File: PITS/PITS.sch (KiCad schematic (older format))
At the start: 48 parts, among them P1 CONN_02X20, P10 I2C, P11 I2C, P12 I2C, P13 I2C, P14 BATT, P2 BNC, P3 BNC, P4 BNC, P5 BNC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

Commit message: board - not finished
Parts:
- P2, P3, P4, P5, P6: footprint Connectors:bnc-ci -> Connectors:SMA_Edge
- U4, U6: footprint RF_Modules:PFM9x -> RF_Modules:RFM9xW
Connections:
- net GPIO12: now also U4.7 (DIO5); no longer U6.7 (DIO5)
- net GPIO16(CE2): now also U4.14 (DIO0); no longer U6.14 (DIO0)
- net GPIO24: now also U6.7 (DIO5); no longer U4.7 (DIO5)
- net GPIO25: now also U6.14 (DIO0); no longer U4.14 (DIO0)
- net GPIO7(CE1): now also U4.5 (nSS); no longer U6.5 (nSS)
- net GPIO8(CE0): now also U6.5 (nSS); no longer U4.5 (nSS)
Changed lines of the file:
@@
 F 0 "U4" H 5700 2350 60  0000 C CNN
 F 1 "RFM9*" H 5700 850 60  0000 C CNN
-F 2 "RF_Modules:PFM9x" H 5800 2800 60  0001 C CNN
+F 2 "RF_Modules:RFM9xW" H 5800 2800 60  0001 C CNN
 F 3 "" H 5800 2800 60  0001 C CNN
 	1    5700 1600
@@
 F 0 "P5" H 4910 1620 50  0000 C CNN
 F 1 "BNC" V 5010 1440 50  0000 C CNN
-F 2 "Connectors:bnc-ci" H 4900 1500 50  0001 C CNN
+F 2 "Connectors:SMA_Edge" H 4900 1500 50  0001 C CNN
 F 3 "" H 4900 1500 50  0000 C CNN
 	1    4900 1500
@@
 F 0 "U6" H 8200 2350 60  0000 C CNN
 F 1 "RFM9*" H 8200 850 60  0000 C CNN
-F 2 "RF_Modules:PFM9x" H 8300 2800 60  0001 C CNN
+F 2 "RF_Modules:RFM9xW" H 8300 2800 60  0001 C CNN
 F 3 "" H 8300 2800 60  0001 C CNN
 	1    8200 1600
@@
 F 0 "P6" H 7410 1620 50  0000 C CNN
 F 1 "BNC" V 7510 1440 50  0000 C CNN
-F 2 "Connectors:bnc-ci" H 7400 1500 50  0001 C CNN
+F 2 "Connectors:SMA_Edge" H 7400 1500 50  0001 C CNN
 F 3 "" H 7400 1500 50  0000 C CNN
 	1    7400 1500
@@
 Text Label 9600 1100 2    60   ~ 0
 GPIO10(MOSI0)
+Text Label 9500 1300 2    60   ~ 0
+GPIO8(CE0)
 Text Label 7000 1300 2    60   ~ 0
-GPIO8(CE0)
-Text Label 9500 1300 2    60   ~ 0
 GPIO7(CE1)
+Text Label 9400 1500 2    60   ~ 0
+GPIO25
+Text Label 9400 2000 2    60   ~ 0
+GPIO24
+Text Label 6900 2000 2    60   ~ 0
+GPIO12
 Text Label 6900 1500 2    60   ~ 0
-GPIO25
-Text Label 6900 2000 2    60   ~ 0
-GPIO24
-Text Label 9400 2000 2    60   ~ 0
-GPIO12
-Text Label 9400 1500 2    60   ~ 0
 GPIO16(CE2)
 Text Notes 9650 2550 2    100  ~ 20
@@
 F 0 "P4" H 3710 6220 50  0000 C CNN
 F 1 "BNC" V 3810 6040 50  0000 C CNN
-F 2 "Connectors:bnc-ci" H 3700 6100 50  0001 C CNN
+F 2 "Connectors:SMA_Edge" H 3700 6100 50  0001 C CNN
 F 3 "" H 3700 6100 50  0000 C CNN
 	1    3700 6100
@@
 F 0 "P3" H 810 6120 50  0000 C CNN
 F 1 "BNC" V 910 5940 50  0000 C CNN
-F 2 "Connectors:bnc-ci" H 800 6000 50  0001 C CNN
+F 2 "Connectors:SMA_Edge" H 800 6000 50  0001 C CNN
 F 3 "" H 800 6000 50  0000 C CNN
 	1    800  6000
@@
 F 0 "P2" H 810 1120 50  0000 C CNN
 F 1 "BNC" V 910 940 50  0000 C CNN
-F 2 "Connectors:bnc-ci" H 800 1000 50  0001 C CNN
+F 2 "Connectors:SMA_Edge" H 800 1000 50  0001 C CNN
 F 3 "" H 800 1000 50  0000 C CNN
 	1    800  1000

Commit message: first finished layout
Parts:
- added U8: BME280, RF_Modules:BME280, symbol BME280
- C1, C14, C2, C4: footprint Capacitors_SMD:C_0805_HandSoldering -> Capacitors_SMD:C_0603_HandSoldering
- D1, D2, D3, D4, D5, D6: footprint LEDs:LED_0805 -> LEDs:LED_0603
- P14: footprint Connectors_Terminal_Blocks:TerminalBlock_Pheonix_MKDS1.5-2pol -> Connectors:SMD_2
- R1, R12, R13, R14, R15, R2, R20, R21, R22, R23, R24, R25, R26, R3, R4, R5, R8: footprint Resistors_SMD:R_0805_HandSoldering -> Resistors_SMD:R_0603_HandSoldering
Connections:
- net +3V3: now also U8.1 (Vin)
- net GND: now also U8.2 (GND)
- net GPIO12: now also U2.4 (TimePulse); no longer U4.7 (DIO5)
- net GPIO16(CE2): now also U2.16 (SDA); no longer U4.14 (DIO0)
- net GPIO19(MISO1): now also U2.17 (SCL); no longer R15.1
- net GPIO2(SDA1): now also U8.4 (SDA)
- net GPIO20(MOSI1): now also R15.1; no longer U2.4 (TimePulse)
- net GPIO22: now also U4.14 (DIO0); no longer U2.17 (SCL)
- net GPIO23: now also U6.7 (DIO5); no longer U1.4 (EN)
- net GPIO24: now also U6.14 (DIO0); no longer U6.7 (DIO5)
- net GPIO25: now also U1.4 (EN); no longer U6.14 (DIO0)
- net GPIO27: now also U4.7 (DIO5); no longer U2.16 (SDA)
- net GPIO3(SCL1): now also U8.3 (SCL)

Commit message: old layout - commit for backup
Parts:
- D3: value INTERNET_Green -> Inet_Green
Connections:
- net GPIO13: now also R21.1; no longer R20.1
- net GPIO16(CE2): now also U2.17 (SCL); no longer U2.16 (SDA)
- net GPIO19(MISO1): now also U2.16 (SDA); no longer U2.17 (SCL)
- net GPIO20(MOSI1): now also R20.1; no longer R15.1
- net GPIO26: now also R22.1; no longer R14.1
- net GPIO5: now also R14.1; no longer R22.1
- net GPIO6: now also R15.1; no longer R21.1
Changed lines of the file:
@@
 P 1200 3700
 F 0 "D3" H 1200 3800 50  0000 C CNN
-F 1 "INTERNET_Green" H 1200 3600 50  0000 C CNN
+F 1 "Inet_Green" H 1200 3600 50  0000 C CNN
 F 2 "LEDs:LED_0603" H 1200 3700 50  0001 C CNN
 F 3 "" H 1200 3700 50  0000 C CNN
@@
 	0    1    1    0
 $EndComp
+Text Label 2800 4500 2    60   ~ 0
+GPIO26
+Text Label 4300 1300 2    60   ~ 0
+GPIO19(MISO1)
+Text Label 2800 4100 2    60   ~ 0
+GPIO13
+Text Label 2800 3300 2    60   ~ 0
+GPIO6
 Text Label 2800 2900 2    60   ~ 0
-GPIO26
-Text Label 4300 1400 2    60   ~ 0
-GPIO19(MISO1)
-Text Label 2800 3700 2    60   ~ 0
-GPIO13
-Text Label 2800 4100 2    60   ~ 0
-GPIO6
-Text Label 2800 4500 2    60   ~ 0
 GPIO5
 Text Label 2800 4900 2    60   ~ 0
@@
 Text Label 3300 6200 2    60   ~ 0
 GPIO25
-Text Label 4300 1300 2    60   ~ 0
+Text Label 4300 1400 2    60   ~ 0
 GPIO16(CE2)
-Text Label 2800 3300 2    60   ~ 0
+Text Label 2800 3700 2    60   ~ 0
 GPIO20(MOSI1)
 Text Label 4100 1600 2    60   ~ 0

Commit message: working on layout
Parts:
- P2, P3, P4, P5, P6: footprint Connectors:SMA_Edge -> Connectors:SMA_Edge_small
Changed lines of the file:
@@
 F 0 "P5" H 4910 1620 50  0000 C CNN
 F 1 "BNC" V 5010 1440 50  0000 C CNN
-F 2 "Connectors:SMA_Edge" H 4900 1500 50  0001 C CNN
+F 2 "Connectors:SMA_Edge_small" H 4900 1500 50  0001 C CNN
 F 3 "" H 4900 1500 50  0000 C CNN
 	1    4900 1500
@@
 F 0 "P6" H 7410 1620 50  0000 C CNN
 F 1 "BNC" V 7510 1440 50  0000 C CNN
-F 2 "Connectors:SMA_Edge" H 7400 1500 50  0001 C CNN
+F 2 "Connectors:SMA_Edge_small" H 7400 1500 50  0001 C CNN
 F 3 "" H 7400 1500 50  0000 C CNN
 	1    7400 1500
@@
 F 0 "P4" H 3710 6220 50  0000 C CNN
 F 1 "BNC" V 3810 6040 50  0000 C CNN
-F 2 "Connectors:SMA_Edge" H 3700 6100 50  0001 C CNN
+F 2 "Connectors:SMA_Edge_small" H 3700 6100 50  0001 C CNN
 F 3 "" H 3700 6100 50  0000 C CNN
 	1    3700 6100
@@
 F 0 "P3" H 810 6120 50  0000 C CNN
 F 1 "BNC" V 910 5940 50  0000 C CNN
-F 2 "Connectors:SMA_Edge" H 800 6000 50  0001 C CNN
+F 2 "Connectors:SMA_Edge_small" H 800 6000 50  0001 C CNN
 F 3 "" H 800 6000 50  0000 C CNN
 	1    800  6000
@@
 F 0 "P2" H 810 1120 50  0000 C CNN
 F 1 "BNC" V 910 940 50  0000 C CNN
-F 2 "Connectors:SMA_Edge" H 800 1000 50  0001 C CNN
+F 2 "Connectors:SMA_Edge_small" H 800 1000 50  0001 C CNN
 F 3 "" H 800 1000 50  0000 C CNN
 	1    800  1000

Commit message: layout - work in progress
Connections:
- net D1: now reaches D1.2 (A), R14.2
- net D2: now reaches D2.2 (A), R15.2
- net D3: now reaches D3.2 (A), R20.2
- net D4: now reaches D4.2 (A), R21.2
- net D5: now reaches D5.2 (A), R22.2
- net D6: now reaches D6.2 (A), R23.2
- net MTX2-TXD: now reaches R2.1, R3.2, R4.2, U3.5 (TXD)
- net HX1-TXD: now reaches R26.2, U1.7 (TXD)
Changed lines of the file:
@@
 Wire Wire Line
 	1800 7300 2500 7300
+Text Label 5400 6000 0    30   ~ 0
+MTX2-TXD
+Text Label 2500 6100 0    30   ~ 0
+HX1-TXD
+Text Label 1500 2900 0    30   ~ 0
+D1
+Text Label 1500 3300 0    30   ~ 0
+D2
+Text Label 1500 3700 0    30   ~ 0
+D3
+Text Label 1500 4100 0    30   ~ 0
+D4
+Text Label 1500 4500 0    30   ~ 0
+D5
+Text Label 1500 4900 0    30   ~ 0
+D6
 $EndSCHEMATC

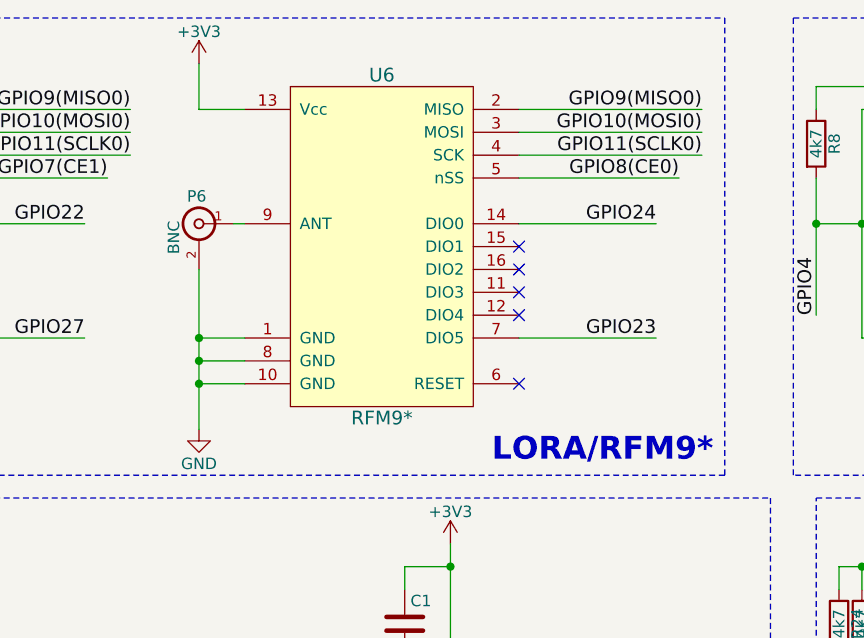
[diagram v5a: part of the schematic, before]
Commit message: layout for zero - work in progress - backup before pin header change
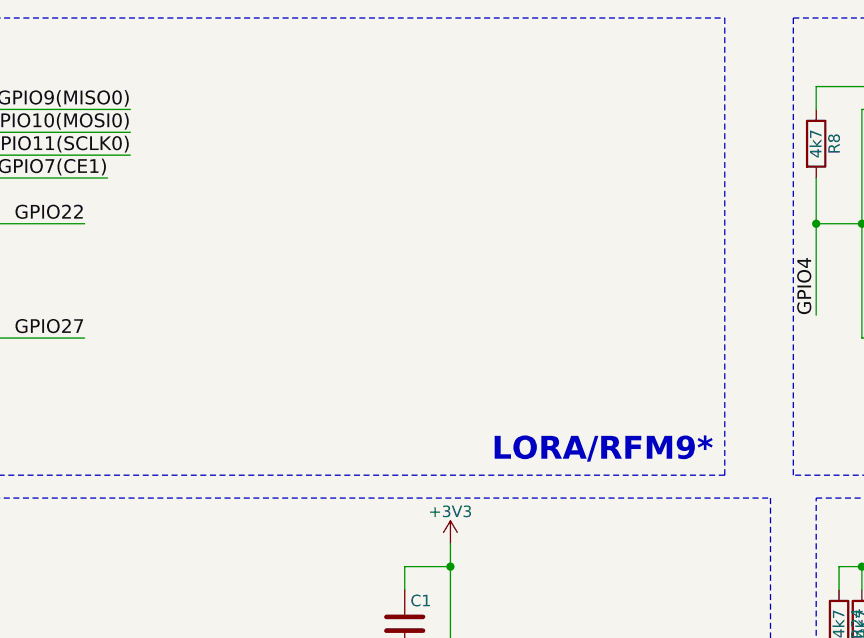
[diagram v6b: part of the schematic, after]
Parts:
- removed P6: BNC, Connectors:SMA_Edge_small, symbol BNC
- removed U6: RFM9*, RF_Modules:RFM9xW, symbol RFM9*
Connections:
- no-connect marks 15 -> 10
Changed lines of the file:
@@
 NoConn ~ 6300 1800
 NoConn ~ 6300 1900
-$Comp
-L RFM9* U6
-U 1 1 581B5A5F
-P 8200 1600
-F 0 "U6" H 8200 2350 60  0000 C CNN
-F 1 "RFM9*" H 8200 850 60  0000 C CNN
-F 2 "RF_Modules:RFM9xW" H 8300 2800 60  0001 C CNN
-F 3 "" H 8300 2800 60  0001 C CNN
-	1    8200 1600
-	1    0    0    -1
-$EndComp
-$Comp
-L +3V3 #PWR016
-U 1 1 581B5A72
-P 7400 800
-F 0 "#PWR016" H 7400 650 50  0001 C CNN
-F 1 "+3V3" H 7400 940 50  0000 C CNN
-F 2 "" H 7400 800 50  0000 C CNN
-F 3 "" H 7400 800 50  0000 C CNN
-	1    7400 800
-	1    0    0    -1
-$EndComp
-$Comp
-L BNC P6
-U 1 1 581B5A7A
-P 7400 1500
-F 0 "P6" H 7410 1620 50  0000 C CNN
-F 1 "BNC" V 7510 1440 50  0000 C CNN
-F 2 "Connectors:SMA_Edge_small" H 7400 1500 50  0001 C CNN
-F 3 "" H 7400 1500 50  0000 C CNN
-	1    7400 1500
-	-1   0    0    -1
-$EndComp
-NoConn ~ 8800 2200
-NoConn ~ 8800 1600
-NoConn ~ 8800 1700
-NoConn ~ 8800 1800
-NoConn ~ 8800 1900
 Text Label 7100 1200 2    60   ~ 0
 GPIO11(SCLK0)
@@
 Text Label 7100 1100 2    60   ~ 0
 GPIO10(MOSI0)
-Text Label 9600 1200 2    60   ~ 0
-GPIO11(SCLK0)
-Text Label 9600 1000 2    60   ~ 0
-GPIO9(MISO0)
-Text Label 9600 1100 2    60   ~ 0
-GPIO10(MOSI0)
-Text Label 9500 1300 2    60   ~ 0
-GPIO8(CE0)
 Text Label 7000 1300 2    60   ~ 0
 GPIO7(CE1)
@@
 $EndComp
 $Comp
-L +3V3 #PWR017
+L +3V3 #PWR016
 U 1 1 581BA557
 P 4700 5500
-F 0 "#PWR017" H 4700 5350 50  0001 C CNN
+F 0 "#PWR016" H 4700 5350 50  0001 C CNN
 F 1 "+3V3" H 4700 5640 50  0000 C CNN
 F 2 "" H 4700 5500 50  0000 C CNN
@@
 $EndComp
 $Comp
-L GND #PWR018
+L GND #PWR017
 U 1 1 581BA55D
 P 4700 6900
-F 0 "#PWR018" H 4700 6650 50  0001 C CNN
+F 0 "#PWR017" H 4700 6650 50  0001 C CNN
 F 1 "GND" H 4700 6750 50  0000 C CNN
 F 2 "" H 4700 6900 50  0000 C CNN
@@
 $EndComp
 $Comp
-L +5V #PWR019
+L +5V #PWR018
 U 1 1 581BA581
 P 1800 5500
-F 0 "#PWR019" H 1800 5350 50  0001 C CNN
+F 0 "#PWR018" H 1800 5350 50  0001 C CNN
 F 1 "+5V" H 1800 5640 50  0000 C CNN
 F 2 "" H 1800 5500 50  0000 C CNN
@@
 $EndComp
 $Comp
-L GND #PWR020
+L GND #PWR019
 U 1 1 581BA587
 P 1800 6800
-F 0 "#PWR020" H 1800 6550 50  0001 C CNN
+F 0 "#PWR019" H 1800 6550 50  0001 C CNN
 F 1 "GND" H 1800 6650 50  0000 C CNN
 F 2 "" H 1800 6800 50  0000 C CNN
@@
 $EndComp
 $Comp
-L GND #PWR021
+L GND #PWR020
 U 1 1 581C3D03
 P 1900 2400
-F 0 "#PWR021" H 1900 2150 50  0001 C CNN
+F 0 "#PWR020" H 1900 2150 50  0001 C CNN
 F 1 "GND" H 1900 2250 50  0000 C CNN
 F 2 "" H 1900 2400 50  0000 C CNN
@@
 NoConn ~ 3500 1700
 $Comp
-L +3V3 #PWR022
+L +3V3 #PWR021
 U 1 1 581C44B1
 P 1900 800
-F 0 "#PWR022" H 1900 650 50  0001 C CNN
+F 0 "#PWR021" H 1900 650 50  0001 C CNN
 F 1 "+3V3" H 1900 940 50  0000 C CNN
 F 2 "" H 1900 800 50  0000 C CNN
@@
 $EndComp
 $Comp
-L GND #PWR023
+L GND #PWR022
 U 1 1 581E58D3
 P 10500 2200
-F 0 "#PWR023" H 10500 1950 50  0001 C CNN
+F 0 "#PWR022" H 10500 1950 50  0001 C CNN
 F 1 "GND" H 10500 2050 50  0000 C CNN
 F 2 "" H 10500 2200 50  0000 C CNN
@@
 $EndComp
 $Comp
-L +3V3 #PWR024
+L +3V3 #PWR023
 U 1 1 581E5D0D
 P 10400 800
-F 0 "#PWR024" H 10400 650 50  0001 C CNN
+F 0 "#PWR023" H 10400 650 50  0001 C CNN
 F 1 "+3V3" H 10400 940 50  0000 C CNN
 F 2 "" H 10400 800 50  0000 C CNN
@@
 	6300 2000 6900 2000
 Wire Wire Line
-	7600 2000 7400 2000
-Wire Wire Line
-	7400 1700 7400 2400
-Wire Wire Line
-	7600 2100 7400 2100
-Connection ~ 7400 2100
-Wire Wire Line
-	7600 2200 7400 2200
-Connection ~ 7400 2200
-Wire Wire Line
-	7400 800  7400 1000
-Wire Wire Line
-	7400 1000 7600 1000
-Connection ~ 7400 2000
-Wire Wire Line
-	7550 1500 7600 1500
-Wire Wire Line
-	8800 2000 9400 2000
-Wire Wire Line
-	8800 1000 9600 1000
-Wire Wire Line
-	8800 1100 9600 1100
-Wire Wire Line
-	8800 1200 9600 1200
-Wire Wire Line
 	7000 1300 6300 1300
-Wire Wire Line
-	9500 1300 8800 1300
 Wire Wire Line
 	4700 6900 4700 6700
@@
 $EndComp
 $Comp
-L +3V3 #PWR025
+L +3V3 #PWR024
 U 1 1 581E8FA4
 P 10400 2900
-F 0 "#PWR025" H 10400 2750 50  0001 C CNN
+F 0 "#PWR024" H 10400 2750 50  0001 C CNN
 F 1 "+3V3" H 10400 3040 50  0000 C CNN
 F 2 "" H 10400 2900 50  0000 C CNN
@@
 $EndComp
 $Comp
-L GND #PWR026
+L GND #PWR025
 U 1 1 581E9036
 P 10500 5600
-F 0 "#PWR026" H 10500 5350 50  0001 C CNN
+F 0 "#PWR025" H 10500 5350 50  0001 C CNN
 F 1 "GND" H 10500 5450 50  0000 C CNN
 F 2 "" H 10500 5600 50  0000 C CNN
@@
 I2C
 $Comp
-L GND #PWR027
-U 1 1 581F0232
-P 7400 2400
-F 0 "#PWR027" H 7400 2150 50  0001 C CNN
-F 1 "GND" H 7400 2250 50  0000 C CNN
-F 2 "" H 7400 2400 50  0000 C CNN
-F 3 "" H 7400 2400 50  0000 C CNN
-	1    7400 2400
-	1    0    0    -1
-$EndComp
-$Comp
-L +3V3 #PWR028
+L +3V3 #PWR026
 U 1 1 581F044F
 P 4900 800
-F 0 "#PWR028" H 4900 650 50  0001 C CNN
+F 0 "#PWR026" H 4900 650 50  0001 C CNN
 F 1 "+3V3" H 4900 940 50  0000 C CNN
 F 2 "" H 4900 800 50  0000 C CNN
@@
 $EndComp
 $Comp
-L +3V3 #PWR029
+L +3V3 #PWR027
 U 1 1 581F1873
 P 3700 1900
-F 0 "#PWR029" H 3700 1750 50  0001 C CNN
+F 0 "#PWR027" H 3700 1750 50  0001 C CNN
 F 1 "+3V3" H 3700 2040 50  0000 C CNN
 F 2 "" H 3700 1900 50  0000 C CNN
@@
 $EndComp
 $Comp
-L GND #PWR030
+L GND #PWR028
 U 1 1 581F2BC2
 P 8100 6100
-F 0 "#PWR030" H 8100 5850 50  0001 C CNN
+F 0 "#PWR028" H 8100 5850 50  0001 C CNN
 F 1 "GND" H 8100 5950 50  0000 C CNN
 F 2 "" H 8100 6100 50  0000 C CNN
@@
 	8100 5900 8100 6100
 $Comp
-L +BATT #PWR031
+L +BATT #PWR029
 U 1 1 581F2E0D
 P 8100 5600
-F 0 "#PWR031" H 8100 5450 50  0001 C CNN
+F 0 "#PWR029" H 8100 5450 50  0001 C CNN
 F 1 "+BATT" H 8100 5740 50  0000 C CNN
 F 2 "" H 8100 5600 50  0000 C CNN
@@
 Wire Wire Line
 	3500 1600 4100 1600
-Wire Wire Line
-	8800 1500 9400 1500
 Text Label 6900 2000 2    60   ~ 0
 GPIO27
 Text Label 6900 1500 2    60   ~ 0
 GPIO22
-Text Label 9400 2000 2    60   ~ 0
-GPIO23
-Text Label 9400 1500 2    60   ~ 0
-GPIO24
 $Comp
 L BME280 U8
@@
 $EndComp
 $Comp
-L GND #PWR032
+L GND #PWR030
 U 1 1 585C2217
 P 900 7600
-F 0 "#PWR032" H 900 7350 50  0001 C CNN
+F 0 "#PWR030" H 900 7350 50  0001 C CNN
 F 1 "GND" H 900 7450 50  0000 C CNN
 F 2 "" H 900 7600 50  0000 C CNN
@@
 $EndComp
 $Comp
-L +3V3 #PWR033
+L +3V3 #PWR031
 U 1 1 585C22B5
 P 900 7200
-F 0 "#PWR033" H 900 7050 50  0001 C CNN
+F 0 "#PWR031" H 900 7050 50  0001 C CNN
 F 1 "+3V3" H 900 7340 50  0000 C CNN
 F 2 "" H 900 7200 50  0000 C CNN

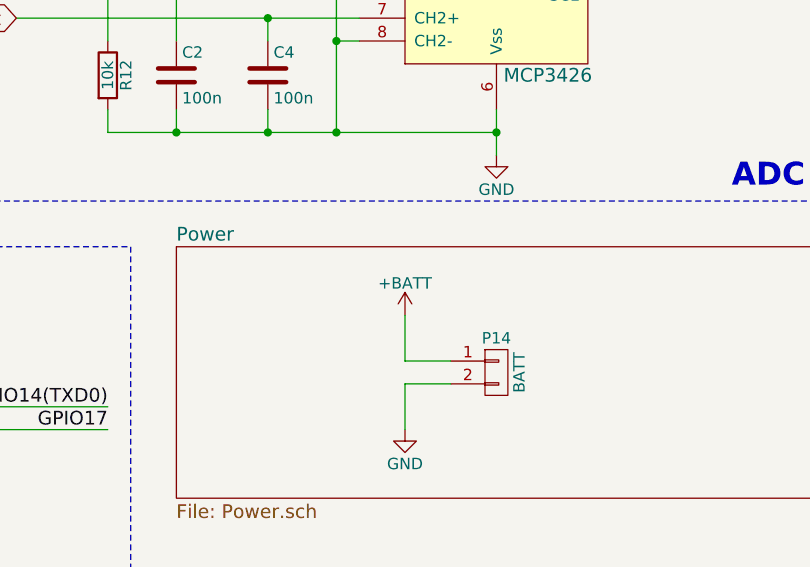
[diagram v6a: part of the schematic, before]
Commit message: layout - work in progress - power net
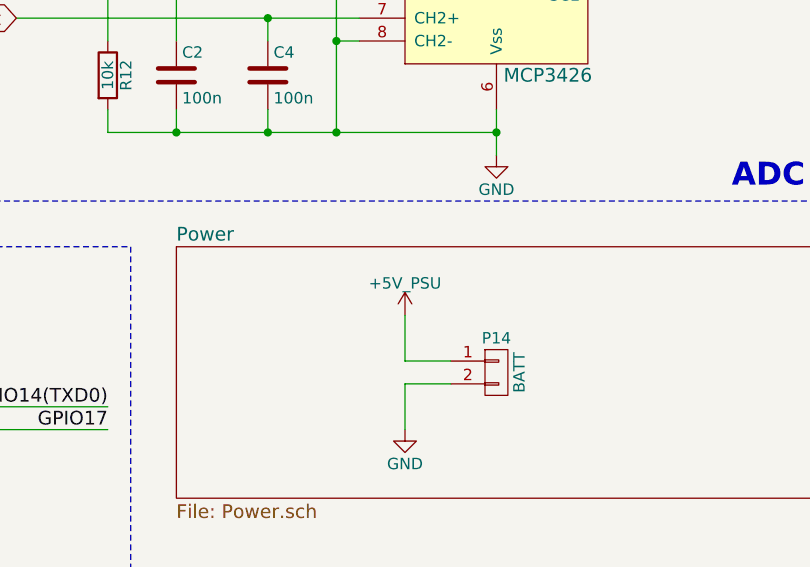
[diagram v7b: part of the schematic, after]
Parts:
- P14: footprint Connectors:SMD_2 -> Connectors:SMD_2_small
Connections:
- net +BATT: no longer P14.1 (P1)
- new net +5V_PSU: P14.1 (P1)
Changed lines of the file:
@@
 F 0 "P14" H 8500 6000 50  0000 C CNN
 F 1 "BATT" V 8600 5850 50  0000 C CNN
-F 2 "Connectors:SMD_2" H 8500 5850 50  0001 C CNN
+F 2 "Connectors:SMD_2_small" H 8500 5850 50  0001 C CNN
 F 3 "" H 8500 5850 50  0000 C CNN
 	1    8500 5850
@@
 Wire Wire Line
 	8100 5900 8100 6100
-$Comp
-L +BATT #PWR029
-U 1 1 581F2E0D
-P 8100 5600
-F 0 "#PWR029" H 8100 5450 50  0001 C CNN
-F 1 "+BATT" H 8100 5740 50  0000 C CNN
-F 2 "" H 8100 5600 50  0000 C CNN
-F 3 "" H 8100 5600 50  0000 C CNN
-	1    8100 5600
-	1    0    0    -1
-$EndComp
 Wire Wire Line
 	8100 5600 8100 5800
@@
 $EndComp
 $Comp
-L GND #PWR030
+L GND #PWR029
 U 1 1 585C2217
 P 900 7600
-F 0 "#PWR030" H 900 7350 50  0001 C CNN
+F 0 "#PWR029" H 900 7350 50  0001 C CNN
 F 1 "GND" H 900 7450 50  0000 C CNN
 F 2 "" H 900 7600 50  0000 C CNN
@@
 $EndComp
 $Comp
-L +3V3 #PWR031
+L +3V3 #PWR030
 U 1 1 585C22B5
 P 900 7200
-F 0 "#PWR031" H 900 7050 50  0001 C CNN
+F 0 "#PWR030" H 900 7050 50  0001 C CNN
 F 1 "+3V3" H 900 7340 50  0000 C CNN
 F 2 "" H 900 7200 50  0000 C CNN
@@
 Text Label 1500 4900 0    30   ~ 0
 D6
+$Comp
+L +5V_PSU #PWR031
+U 1 1 5990B289
+P 8100 5600
+F 0 "#PWR031" H 8100 5450 50  0001 C CNN
+F 1 "+5V_PSU" H 8100 5740 50  0000 C CNN
+F 2 "" H 8100 5600 50  0000 C CNN
+F 3 "" H 8100 5600 50  0000 C CNN
+	1    8100 5600
+	1    0    0    -1
+$EndComp
 $EndSCHEMATC
